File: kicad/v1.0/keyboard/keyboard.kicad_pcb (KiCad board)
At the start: 2 copper layers, 124 parts, among them J1 NumPad, J2 PMOD, SW1 KeyButton, SW10 KeyButton, SW11 KeyButton, SW12 KeyButton, SW13 KeyButton, SW14 KeyButton, SW15 KeyButton, SW16 KeyButton, SW17 KeyButton, SW18 KeyButton, SW19 KeyButton, SW2 KeyButton, SW20 KeyButton, SW21 KeyButton, SW22 KeyButton, SW23 KeyButton, SW24 KeyButton, SW25 KeyButton, SW26 KeyButton, SW27 KeyButton, SW3 KeyButton, SW33 KeyButton, SW34 KeyButton, SW35 KeyButton, SW36 KeyButton, SW37 KeyButton, SW38 KeyButton, SW39 KeyButton, SW4 KeyButton, SW40 KeyButton, SW41 KeyButton, SW42 KeyButton, SW43 KeyButton, SW44 KeyButton, SW45 KeyButton, SW46 KeyButton, SW47 KeyButton, SW48 KeyButton, SW49 KeyButton, SW5 KeyButton, SW50 KeyButton, SW51 KeyButton, SW52 KeyButton, SW53 KeyButton, SW54 KeyButton, SW55 KeyButton, SW56 KeyButton, SW57 KeyButton, SW58 KeyButton, SW59 KeyButton, SW6 KeyButton, SW7 KeyButton, SW8 KeyButton, SW9 KeyButton, U1 74LS165, U2 74LS165, U3 74LS165, U4 74LS165, U5 74LS165, U6 74LS165, U7 74LS165

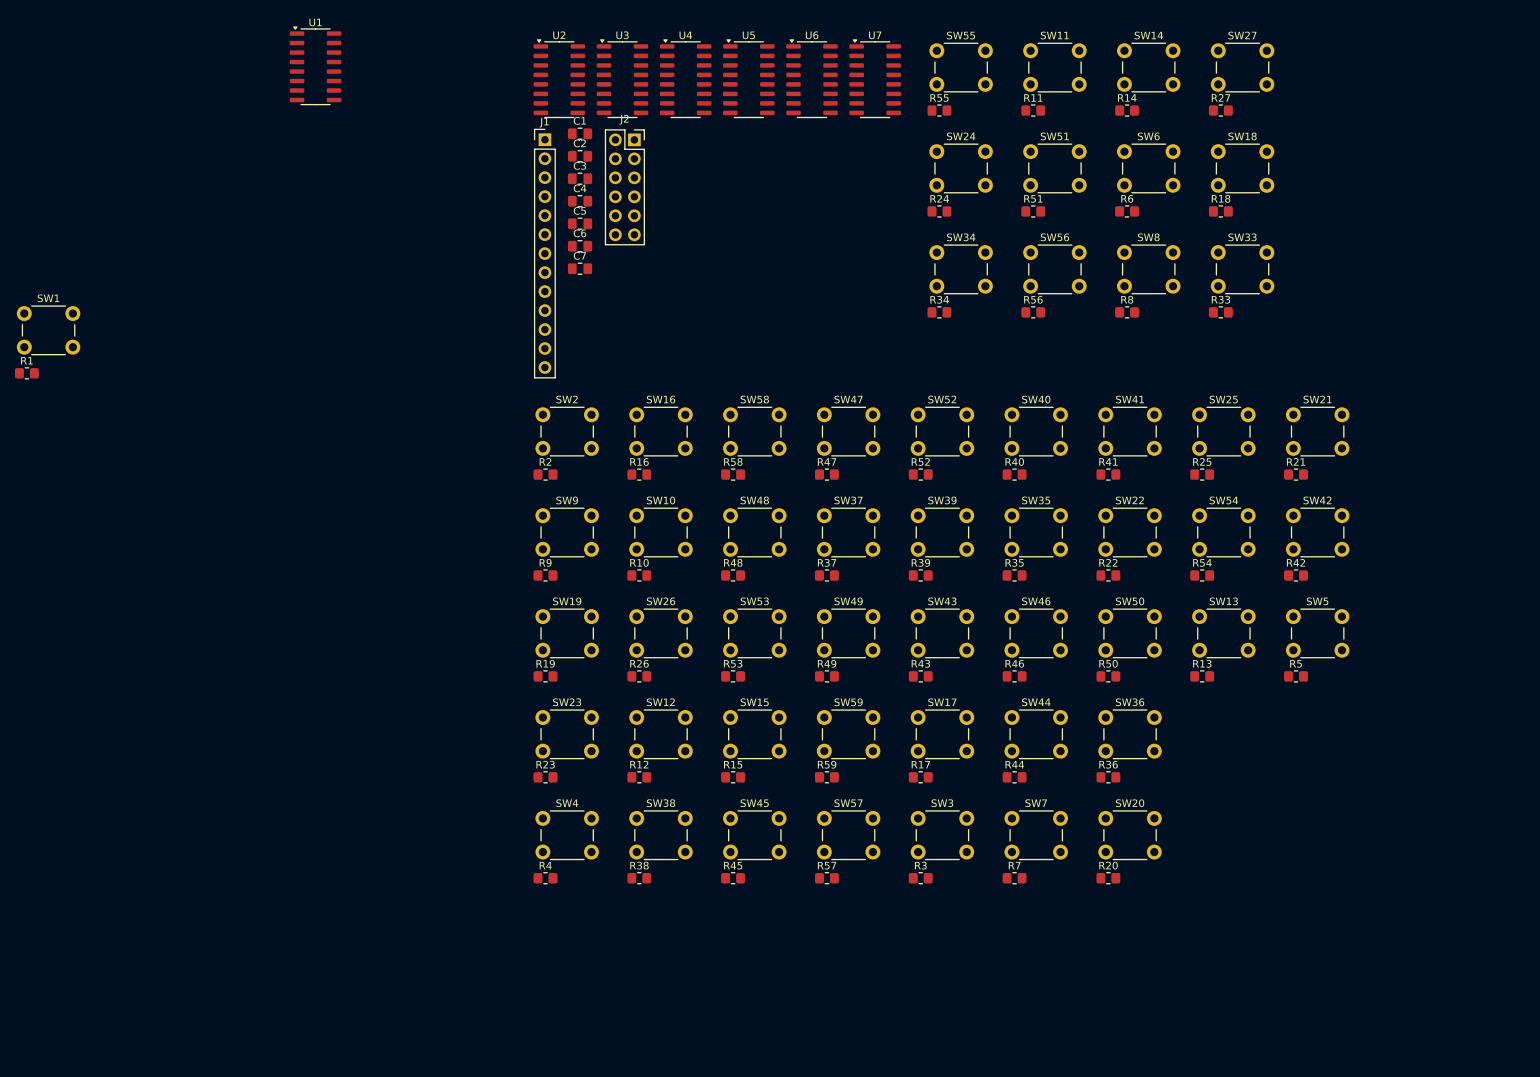
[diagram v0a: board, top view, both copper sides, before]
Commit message: Positioning
- Added Library
- Created Footprint for 2-pin push-button
- Added additional keys for ENTER and SPACE to cover whole length
- Added keys for numpad (1:1 link to other number keys)
- Positioned main keys, numpad keys
- Created cutout for reset switch
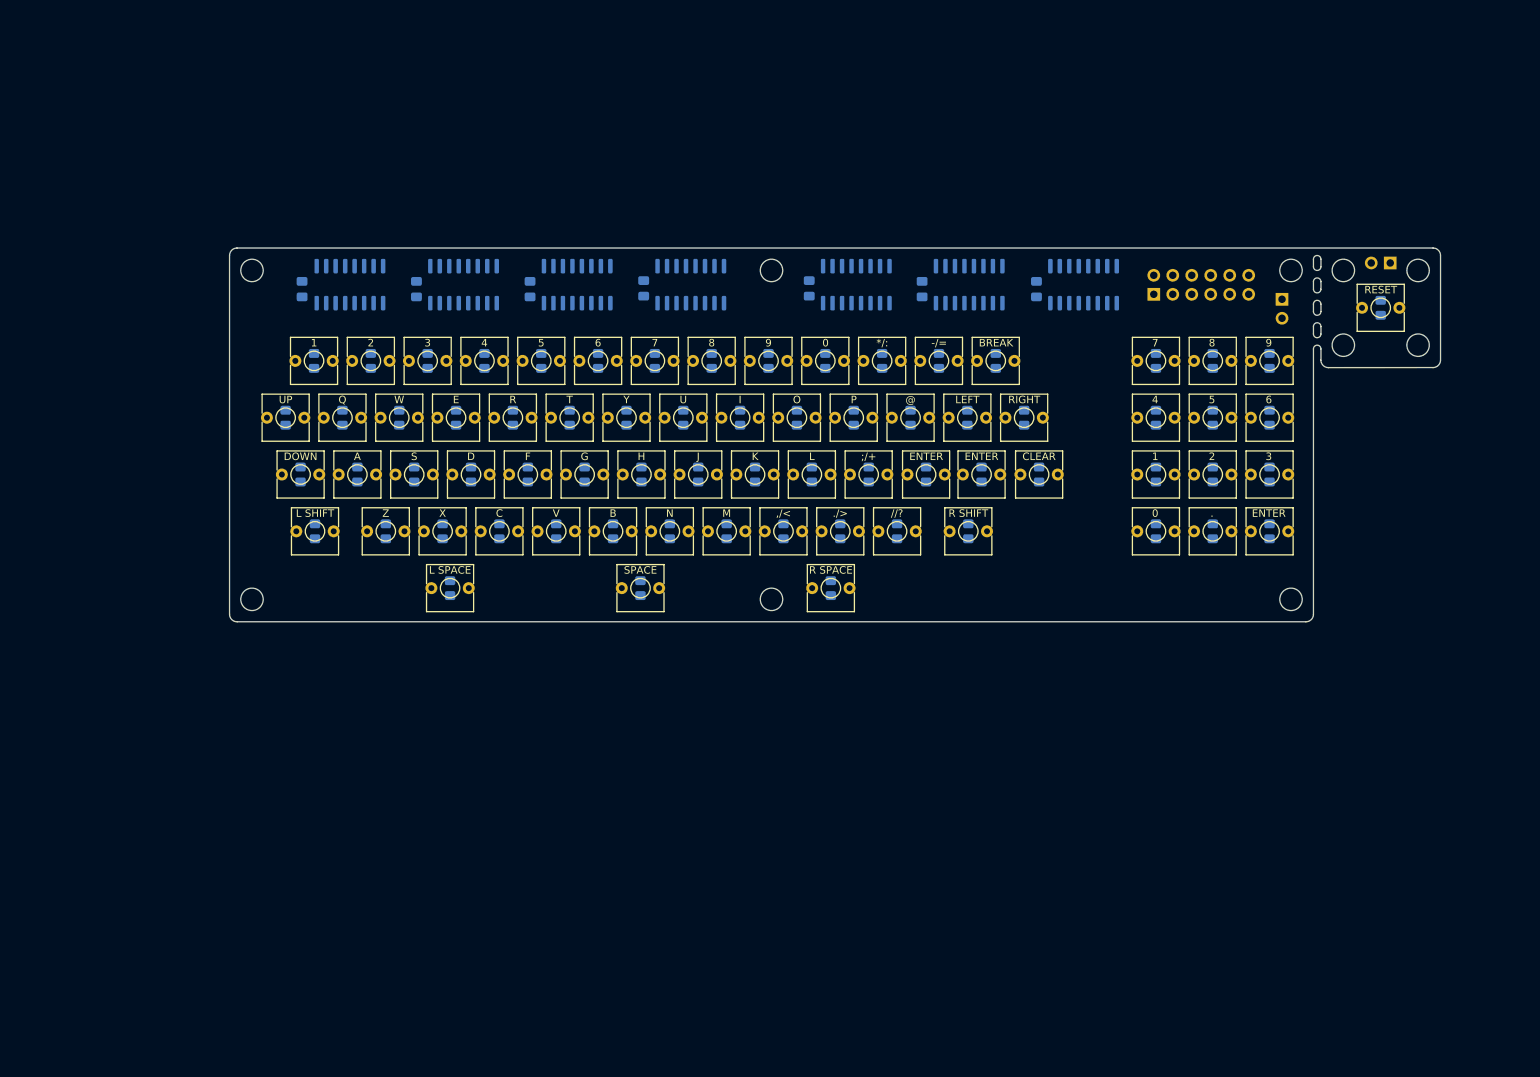
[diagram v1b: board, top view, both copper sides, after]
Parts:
- added J3: Conn_01x02, Connector_PinHeader_2.54mm:PinHeader_1x02_P2.54mm_Vertical, B.Cu at (224.5, 75.5)
- added R60: 4K7, Resistor_SMD:R_0805_2012Metric_Pad1.20x1.40mm_HandSolder, B.Cu at (169.9, 103.8)
- added R61: 4K7, Resistor_SMD:R_0805_2012Metric_Pad1.20x1.40mm_HandSolder, B.Cu at (124.2, 119.0)
- added R62: 4K7, Resistor_SMD:R_0805_2012Metric_Pad1.20x1.40mm_HandSolder, B.Cu at (149.7, 119.0)
- added R63: 4K7, Resistor_SMD:R_0805_2012Metric_Pad1.20x1.40mm_HandSolder, B.Cu at (193.2, 103.8)
- added R64: 4K7, Resistor_SMD:R_0805_2012Metric_Pad1.20x1.40mm_HandSolder, B.Cu at (193.2, 111.4)
- added R65: 4K7, Resistor_SMD:R_0805_2012Metric_Pad1.20x1.40mm_HandSolder, B.Cu at (200.8, 103.8)
- added R66: 4K7, Resistor_SMD:R_0805_2012Metric_Pad1.20x1.40mm_HandSolder, B.Cu at (208.4, 103.8)
- added R67: 4K7, Resistor_SMD:R_0805_2012Metric_Pad1.20x1.40mm_HandSolder, B.Cu at (193.2, 96.2)
- added R68: 4K7, Resistor_SMD:R_0805_2012Metric_Pad1.20x1.40mm_HandSolder, B.Cu at (200.8, 96.2)
- added R69: 4K7, Resistor_SMD:R_0805_2012Metric_Pad1.20x1.40mm_HandSolder, B.Cu at (208.4, 96.2)
- added R70: 4K7, Resistor_SMD:R_0805_2012Metric_Pad1.20x1.40mm_HandSolder, B.Cu at (193.2, 88.6)
- added R71: 4K7, Resistor_SMD:R_0805_2012Metric_Pad1.20x1.40mm_HandSolder, B.Cu at (208.4, 88.6)
- added R72: 4K7, Resistor_SMD:R_0805_2012Metric_Pad1.20x1.40mm_HandSolder, B.Cu at (200.8, 88.6)
- added R73: 4K7, Resistor_SMD:R_0805_2012Metric_Pad1.20x1.40mm_HandSolder, B.Cu at (200.8, 111.4)
- added R74: 4K7, Resistor_SMD:R_0805_2012Metric_Pad1.20x1.40mm_HandSolder, B.Cu at (208.4, 111.4)
- added SW60: KeyButton, Library:SW_SPST_Push, F.Cu at (169.9, 103.8)
- added SW61: KeyButton, Library:SW_SPST_Push, F.Cu at (124.2, 119.0)
- added SW62: KeyButton, Library:SW_SPST_Push, F.Cu at (149.7, 119.0)
- added SW63: KeyButton, Library:SW_SPST_Push, F.Cu at (193.2, 103.8)
- added SW64: KeyButton, Library:SW_SPST_Push, F.Cu at (193.2, 111.4)
- added SW65: KeyButton, Library:SW_SPST_Push, F.Cu at (200.8, 103.8)
- added SW66: KeyButton, Library:SW_SPST_Push, F.Cu at (208.4, 103.8)
- added SW67: KeyButton, Library:SW_SPST_Push, F.Cu at (193.2, 96.2)
- added SW68: KeyButton, Library:SW_SPST_Push, F.Cu at (200.8, 96.2)
- added SW69: KeyButton, Library:SW_SPST_Push, F.Cu at (208.4, 96.2)
- added SW70: KeyButton, Library:SW_SPST_Push, F.Cu at (193.2, 88.6)
- added SW71: KeyButton, Library:SW_SPST_Push, F.Cu at (208.4, 88.6)
- added SW72: KeyButton, Library:SW_SPST_Push, F.Cu at (200.8, 88.6)
- added SW73: KeyButton, Library:SW_SPST_Push, F.Cu at (200.8, 111.4)
- added SW74: KeyButton, Library:SW_SPST_Push, F.Cu at (208.4, 111.4)
- C1, C2, C3, C4, C5, C6, C7, R1, R10, R11, R12, R13, R14, R15, R16, R17, R18, R19, R2, R20, R21, R22, R23, R24, R25, R26, R27, R3, R33, R34, R35, R36, R37, R38, R39, R4, R40, R41, R42, R43, R44, R45, R46, R47, R48, R49, R5, R50, R51, R52, R53, R54, R55, R56, R57, R58, R59, R6, R7, R8, R9, U1, U2, U3, U4, U5, U6, U7: moved to B.Cu
- J1: value NumPad -> PMOD; footprint Connector_PinHeader_2.54mm:PinHeader_1x13_P2.54mm_Vertical -> Connector_PinSocket_2.54mm:PinSocket_2x06_P2.54mm_Vertical; moved to B.Cu
- J2: value PMOD -> Conn_01x02; footprint Connector_PinSocket_2.54mm:PinSocket_2x06_P2.54mm_Vertical -> Connector_PinHeader_2.54mm:PinHeader_1x02_P2.54mm_Vertical; moved to B.Cu
- SW1, SW10, SW11, SW12, SW13, SW14, SW15, SW16, SW17, SW18, SW19, SW2, SW20, SW21, SW22, SW23, SW24, SW25, SW26, SW27, SW3, SW33, SW34, SW35, SW36, SW37, SW38, SW39, SW4, SW40, SW41, SW42, SW43, SW44, SW45, SW46, SW47, SW48, SW49, SW5, SW50, SW51, SW52, SW53, SW54, SW55, SW56, SW57, SW58, SW59, SW6, SW7, SW8, SW9: footprint Button_Switch_THT:SW_PUSH_6mm -> Library:SW_SPST_Push
- moved SW27 128.6 mm to (90.2, 111.4)
- moved R27 125.1 mm to (90.2, 111.4), turned to 90 degrees
- moved SW33 121.8 mm to (80.6, 88.6)
- moved R33 121.5 mm to (80.6, 88.6), turned to 90 degrees
- moved SW1 119.4 mm to (160.4, 96.2)
- moved R1 118.4 mm to (160.4, 96.2), turned to 90 degrees
- moved R5 113.6 mm to (101.6, 103.8), turned to 90 degrees
- moved SW5 111.6 mm to (101.6, 103.8)
- moved R20 107.4 mm to (94.0, 103.8), turned to 90 degrees
- moved R36 106.8 mm to (95.8, 88.6), turned to 90 degrees
- moved SW20 103.3 mm to (94.0, 103.8)
- moved SW36 102.5 mm to (95.8, 88.6)
- moved R21 97.5 mm to (114.8, 96.2), turned to 90 degrees
- moved R59 97.1 mm to (223.3, 81.5), turned to 90 degrees
- moved SW21 96.8 mm to (114.8, 96.2)
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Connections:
- J1 pad 1: unconnected-(J1-Pin_1-Pad1) -> PMOD_IO1
- J1 pad 10: unconnected-(J1-Pin_10-Pad10) -> GND
- J1 pad 11: unconnected-(J1-Pin_11-Pad11) -> +3V3
- J1 pad 12: unconnected-(J1-Pin_12-Pad12) -> +3V3
- J1 pad 2: unconnected-(J1-Pin_2-Pad2) -> PMOD_IO5
- J1 pad 3: unconnected-(J1-Pin_3-Pad3) -> PMOD_IO2
- J1 pad 4: unconnected-(J1-Pin_4-Pad4) -> PMOD_IO6
- J1 pad 5: unconnected-(J1-Pin_5-Pad5) -> PMOD_IO3
- J1 pad 6: unconnected-(J1-Pin_6-Pad6) -> PMOD_IO7
- J1 pad 7: unconnected-(J1-Pin_7-Pad7) -> PMOD_IO4
- J1 pad 8: unconnected-(J1-Pin_8-Pad8) -> PMOD_IO8
- J1 pad 9: unconnected-(J1-Pin_9-Pad9) -> GND
- J2 pad 1: PMOD_IO1 -> unconnected-(J2-Pin_1-Pad1)
- J2 pad 2: PMOD_IO5 -> GND
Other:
- board outline added: 162 x 50 mm
- board text added: "*/:"
- board text added: ",/<"
- board text added: "-/="
- board text added: "."
- board text added: "./>"
- board text added: "//?"
- board text added: "0"
- board text added: "1"
- board text added: "2"
- board text added: "3"
- board text added: "4"
- board text added: "5"
- board text added: "6"
- board text added: "7"
- board text added: "8"
- board text added: "9"
- board text added: ";/+"
- board text added: "@"
- board text added: "A"
- board text added: "B"
- board text added: "BREAK"
- board text added: "C"
- board text added: "CLEAR"
- board text added: "D"
- board text added: "DOWN"
- board text added: "E"
- board text added: "ENTER"
- board text added: "F"
- board text added: "G"
- board text added: "H"
- board text added: "I"
- board text added: "J"
- board text added: "K"
- board text added: "L"
- board text added: "L SHIFT"
- board text added: "L SPACE"
- board text added: "LEFT"
- board text added: "M"
- board text added: "N"
- board text added: "O"
- board text added: "P"
- board text added: "Q"
- board text added: "R"
- board text added: "R SHIFT"
- board text added: "R SPACE"
- board text added: "RESET"
- board text added: "RIGHT"
- board text added: "S"
- board text added: "SPACE"
- board text added: "T"
- board text added: "U"
- board text added: "UP"
- board text added: "V"
- board text added: "W"
- board text added: "X"
- board text added: "Y"
- board text added: "Z"

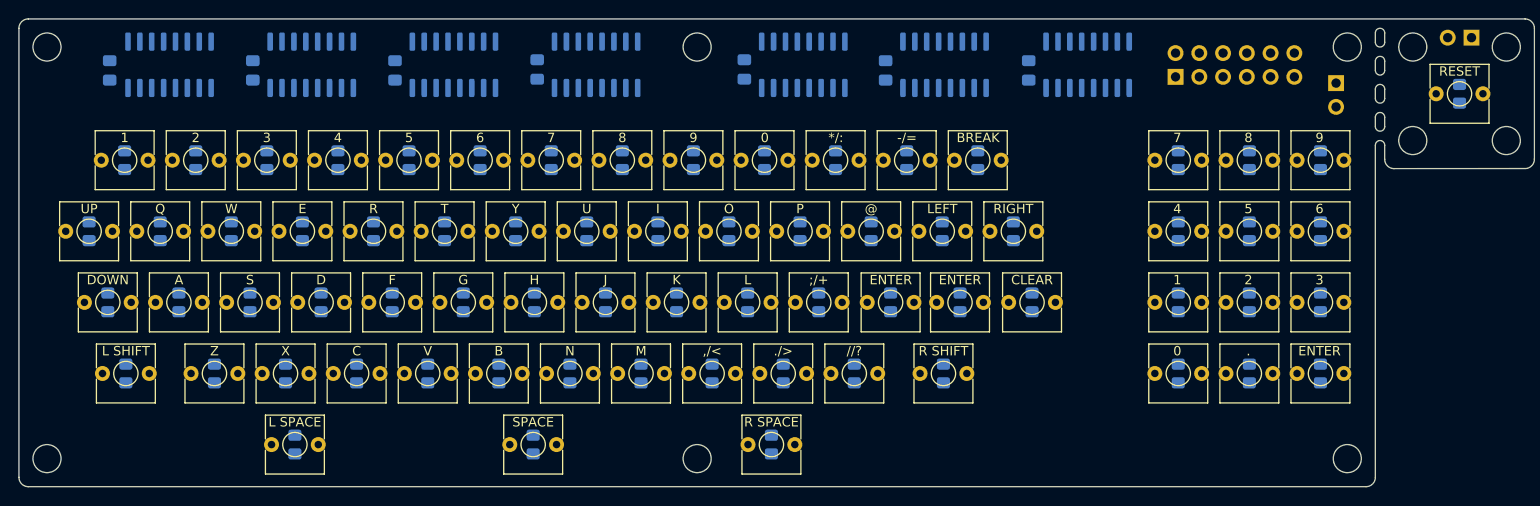
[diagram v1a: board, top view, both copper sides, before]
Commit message: Redesign of Keyboard
This is a new design of the keyboard that is based on the TRS-80 Model 1 keyboard interface design.
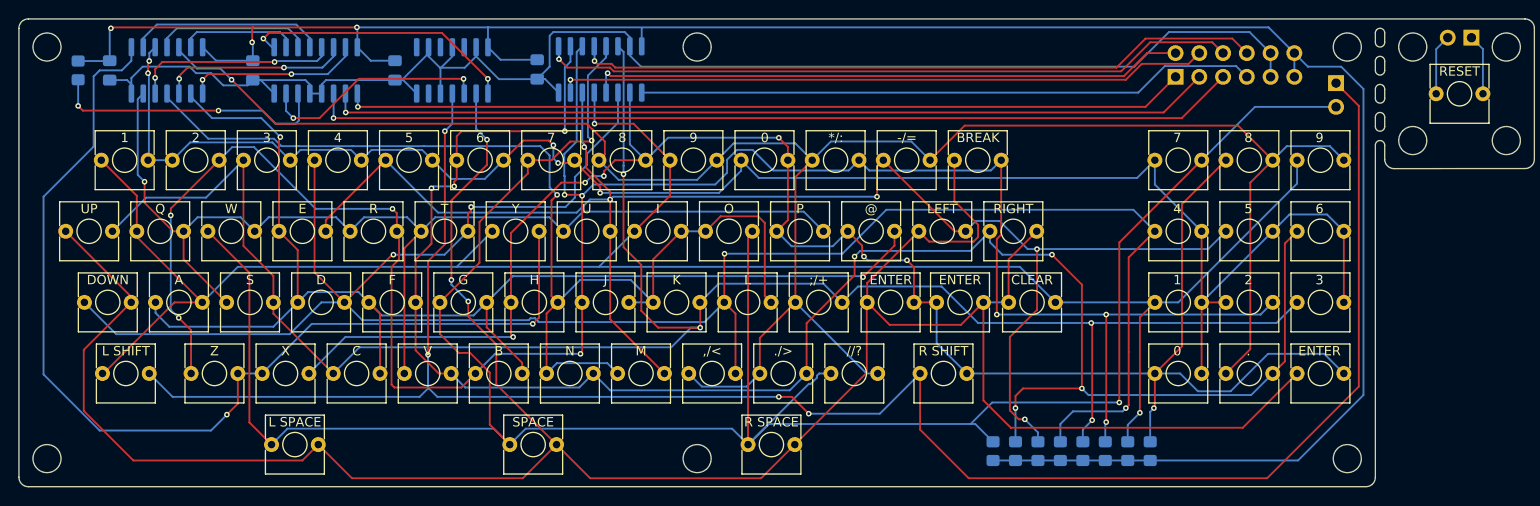
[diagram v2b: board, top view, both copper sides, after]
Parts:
- removed C5, C6, C7: 0.1uF, Capacitor_SMD:C_0805_2012Metric_Pad1.18x1.45mm_HandSolder
- removed R10, R11, R12, R13, R14, R15, R16, R17, R18, R19, R20, R21, R22, R23, R24, R25, R26, R27, R33, R34, R35, R36, R37, R38, R39, R40, R41, R42, R43, R44, R45, R46, R47, R48, R49, R50, R51, R52, R53, R54, R55, R56, R57, R58, R59, R60, R61, R62, R63, R64, R65, R66, R67, R68, R69, R70, R71, R72, R73, R74: 4K7, Resistor_SMD:R_0805_2012Metric_Pad1.20x1.40mm_HandSolder
- removed U5, U6, U7: 74LS165, Package_SO:SOIC-16_3.9x9.9mm_P1.27mm
- R1, R2, R3, R4, R5, R6, R7, R8, R9: value 4K7 -> 1k
- SW1: value KeyButton -> @
- SW10: renamed from SW9; value KeyButton -> I
- SW11: value KeyButton -> J
- SW12: value KeyButton -> K
- SW13: value KeyButton -> L
- SW14: value KeyButton -> M
- SW15: value KeyButton -> N
- SW16: value KeyButton -> O
- SW17: renamed from SW18; value KeyButton -> P
- SW18: renamed from SW17; value KeyButton -> Q
- SW19: value KeyButton -> R
- SW2: value KeyButton -> A
- SW20: value KeyButton -> S
- SW21: value KeyButton -> T
- SW22: value KeyButton -> U
- SW23: value KeyButton -> V
- SW24: value KeyButton -> W
- SW25: renamed from SW26; value KeyButton -> X
- SW26: renamed from SW25; value KeyButton -> Y
- SW27: value KeyButton -> Z
- SW28: renamed from SW64; value KeyButton -> 0
- SW29: renamed from SW63; value KeyButton -> 1
- SW3: value KeyButton -> B
- SW30: renamed from SW65; value KeyButton -> 2
- SW31: renamed from SW66; value KeyButton -> 3
- SW32: renamed from SW67; value KeyButton -> 4
- SW33: renamed from SW68; value KeyButton -> 5
- SW34: renamed from SW69; value KeyButton -> 6
- SW35: renamed from SW70; value KeyButton -> 7
- SW36: renamed from SW34; value KeyButton -> 0
- SW37: renamed from SW33; value KeyButton -> 1
- SW38: renamed from SW35; value KeyButton -> 2
- SW39: renamed from SW36; value KeyButton -> 3
- SW4: value KeyButton -> C
- SW40: renamed from SW37; value KeyButton -> 4
- SW41: renamed from SW38; value KeyButton -> 5
- SW42: renamed from SW39; value KeyButton -> 6
- SW43: renamed from SW40; value KeyButton -> 7
- SW44: renamed from SW72; value KeyButton -> 8
- SW45: renamed from SW71; value KeyButton -> 9
- SW46: renamed from SW73; value KeyButton -> .
- SW47: renamed from SW42; value KeyButton -> 8
- SW48: renamed from SW41; value KeyButton -> 9
- SW49: renamed from SW43; value KeyButton -> :
- SW5: value KeyButton -> D
- SW50: renamed from SW44; value KeyButton -> ;
- SW51: renamed from SW45; value KeyButton -> ,
- SW52: renamed from SW46; value KeyButton -> -
- SW53: renamed from SW47; value KeyButton -> .
- SW54: renamed from SW48; value KeyButton -> /
- SW55: renamed from SW50; value KeyButton -> ENTER
- SW56: renamed from SW60; value KeyButton -> ENTER
- SW57: renamed from SW49; value KeyButton -> CLEAR
- SW58: renamed from SW51; value KeyButton -> BREAK
- SW59: renamed from SW52; value KeyButton -> UP
- SW6: value KeyButton -> E
- SW60: renamed from SW53; value KeyButton -> DOWN
- SW61: renamed from SW54; value KeyButton -> LEFT
- SW62: renamed from SW55; value KeyButton -> RIGHT
- SW63: renamed from SW61; value KeyButton -> SPACE
- SW64: renamed from SW59; value KeyButton -> RESET
- SW65: renamed from SW57; value KeyButton -> RSHIFT
- SW66: renamed from SW58; value KeyButton -> LSHIFT
- SW67: renamed from SW56; value KeyButton -> SPACE
- SW68: renamed from SW62; value KeyButton -> SPACE
- SW69: renamed from SW74; value KeyButton -> ENTER
- SW7: value KeyButton -> F
- SW8: value KeyButton -> G
- SW9: renamed from SW10; value KeyButton -> H
- U1, U3: value 74LS165 -> 74LS07; footprint Package_SO:SOIC-16_3.9x9.9mm_P1.27mm -> Package_SO:SOIC-14_3.9x8.7mm_P1.27mm
- U2: value 74LS165 -> 74LS138
- U4: value 74LS165 -> 74LS157
- moved R2 105.0 mm to (190.2, 119.7)
- moved R1 86.5 mm to (75.6, 79.0), turned to -90 degrees
- moved R6 84.4 mm to (180.6, 119.7)
- moved R5 83.0 mm to (183.0, 119.7)
- moved R4 80.5 mm to (185.4, 119.7)
- moved R7 70.8 mm to (178.2, 119.7)
- moved R3 67.7 mm to (187.8, 119.7)
- moved R8 61.1 mm to (175.8, 119.7)
- moved R9 42.8 mm to (173.4, 119.7)
- moved U2 0.74 mm to (101.0, 79.0), turned to 90 degrees
- moved U4 0.66 mm to (131.4, 78.9), turned to 90 degrees
- moved U1 0.66 mm to (85.1, 79.0), turned to 90 degrees
- moved U3 0.62 mm to (115.6, 79.0), turned to 90 degrees
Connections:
- net KEY_RESET renamed Net-(J3-Pin_1)
- C1 pad 1: GND -> +3.3V
- C1 pad 2: +3V3 -> GND
- C2 pad 1: GND -> +3.3V
- C2 pad 2: +3V3 -> GND
- C3 pad 1: GND -> +3.3V
- C3 pad 2: +3V3 -> GND
- C4 pad 1: GND -> +3.3V
- C4 pad 2: +3V3 -> GND
- J1 pad 11: +3V3 -> +3.3V
- J1 pad 12: +3V3 -> +3.3V
- J2 pad 1: unconnected-(J2-Pin_1-Pad1) -> Net-(J2-Pin_1)
- J2 pad 2: GND -> Net-(J2-Pin_2)
- J3 pad 2: GND -> Net-(J3-Pin_2)
- R1 pad 1: +3V3 -> +3.3V
- R1 pad 2: KEY_AT -> Net-(U2-E3)
- R2 pad 1: +3V3 -> +3.3V
- R2 pad 2: KEY_A -> Net-(U4-I0a)
- R3 pad 1: +3V3 -> +3.3V
- R3 pad 2: KEY_B -> Net-(U4-I0b)
- R4 pad 1: +3V3 -> +3.3V
- R4 pad 2: KEY_C -> Net-(U4-I0c)
- R5 pad 1: +3V3 -> +3.3V
- R5 pad 2: KEY_D -> Net-(U4-I0d)
- R6 pad 1: +3V3 -> +3.3V
- R6 pad 2: KEY_E -> Net-(U4-I1a)
- R7 pad 1: +3V3 -> +3.3V
- R7 pad 2: KEY_F -> Net-(U4-I1b)
- R8 pad 1: +3V3 -> +3.3V
- R8 pad 2: KEY_G -> Net-(U4-I1c)
- R9 pad 1: +3V3 -> +3.3V
- R9 pad 2: KEY_I -> Net-(J2-Pin_2)
- SW1 pad 1: GND -> Net-(U4-I0a)
- SW1 pad 2: KEY_AT -> Net-(SW1-Pad2)
- SW10 pad 1: GND -> Net-(U4-I0b)
- SW10 pad 2: KEY_I -> Net-(SW10-Pad2)
- SW11 pad 1: GND -> Net-(U4-I0c)
- SW11 pad 2: KEY_J -> Net-(SW10-Pad2)
- SW12 pad 1: GND -> Net-(SW10-Pad2)
- SW12 pad 2: KEY_K -> Net-(U4-I0d)
- SW13 pad 1: GND -> Net-(U4-I1a)
- SW13 pad 2: KEY_L -> Net-(SW10-Pad2)
- SW14 pad 1: GND -> Net-(SW10-Pad2)
- SW14 pad 2: KEY_M -> Net-(U4-I1b)
- SW15 pad 1: GND -> Net-(SW10-Pad2)
- SW15 pad 2: KEY_N -> Net-(U4-I1c)
- SW16 pad 1: GND -> Net-(SW10-Pad2)
- SW16 pad 2: KEY_O -> Net-(J2-Pin_2)
- SW17 pad 1: GND -> Net-(U4-I0a)
- SW17 pad 2: KEY_P -> Net-(SW17-Pad2)
- SW18 pad 1: GND -> Net-(U4-I0b)
- SW18 pad 2: KEY_Q -> Net-(SW17-Pad2)
- SW19 pad 1: GND -> Net-(SW17-Pad2)
- SW19 pad 2: KEY_R -> Net-(U4-I0c)
- SW2 pad 1: GND -> Net-(SW1-Pad2)
- SW2 pad 2: KEY_A -> Net-(U4-I0b)
- SW20 pad 1: GND -> Net-(SW17-Pad2)
- SW20 pad 2: KEY_S -> Net-(U4-I0d)
- SW21 pad 1: GND -> Net-(SW17-Pad2)
- SW21 pad 2: KEY_T -> Net-(U4-I1a)
- SW22 pad 1: GND -> Net-(SW17-Pad2)
- SW22 pad 2: KEY_U -> Net-(U4-I1b)
- SW23 pad 1: GND -> Net-(SW17-Pad2)
- SW23 pad 2: KEY_V -> Net-(U4-I1c)
- SW24 pad 1: GND -> Net-(J2-Pin_2)
- SW24 pad 2: KEY_W -> Net-(SW17-Pad2)
- SW25 pad 1: GND -> Net-(SW25-Pad1)
- SW25 pad 2: KEY_X -> Net-(U4-I0a)
- SW26 pad 1: GND -> Net-(U4-I0b)
- SW26 pad 2: KEY_Y -> Net-(SW25-Pad1)
- SW27 pad 1: GND -> Net-(U4-I0c)
- SW27 pad 2: KEY_Z -> Net-(SW25-Pad1)
- SW28 pad 1: GND -> Net-(U4-I0a)
- SW28 pad 2: KEY_0 -> Net-(SW28-Pad2)
- SW29 pad 1: GND -> Net-(U4-I0b)
- SW29 pad 2: KEY_1 -> Net-(SW28-Pad2)
- SW3 pad 1: GND -> Net-(U4-I0c)
- SW3 pad 2: KEY_B -> Net-(SW1-Pad2)
- SW30 pad 1: GND -> Net-(SW28-Pad2)
- SW30 pad 2: KEY_2 -> Net-(U4-I0c)
- SW31 pad 1: GND -> Net-(U4-I0d)
- SW31 pad 2: KEY_3 -> Net-(SW28-Pad2)
- SW32 pad 1: GND -> Net-(U4-I1a)
- SW32 pad 2: KEY_4 -> Net-(SW28-Pad2)
- SW33 pad 1: GND -> Net-(U4-I1b)
- SW33 pad 2: KEY_5 -> Net-(SW28-Pad2)
- SW34 pad 1: GND -> Net-(U4-I1c)
- SW34 pad 2: KEY_6 -> Net-(SW28-Pad2)
- SW35 pad 1: GND -> Net-(SW28-Pad2)
- SW35 pad 2: KEY_7 -> Net-(J2-Pin_2)
- SW36 pad 1: GND -> Net-(SW28-Pad2)
- SW36 pad 2: KEY_0 -> Net-(U4-I0a)
- SW37 pad 1: GND -> Net-(U4-I0b)
- SW37 pad 2: KEY_1 -> Net-(SW28-Pad2)
- SW38 pad 1: GND -> Net-(SW28-Pad2)
- SW38 pad 2: KEY_2 -> Net-(U4-I0c)
- SW39 pad 1: GND -> Net-(U4-I0d)
- SW39 pad 2: KEY_3 -> Net-(SW28-Pad2)
- SW4 pad 1: GND -> Net-(U4-I0d)
- SW4 pad 2: KEY_C -> Net-(SW1-Pad2)
- SW40 pad 1: GND -> Net-(U4-I1a)
- SW40 pad 2: KEY_4 -> Net-(SW28-Pad2)
- SW41 pad 1: GND -> Net-(U4-I1b)
- SW41 pad 2: KEY_5 -> Net-(SW28-Pad2)
- SW42 pad 1: GND -> Net-(U4-I1c)
- SW42 pad 2: KEY_6 -> Net-(SW28-Pad2)
- SW43 pad 1: GND -> Net-(J2-Pin_2)
- SW43 pad 2: KEY_7 -> Net-(SW28-Pad2)
- SW44 pad 1: GND -> Net-(U4-I0a)
- SW44 pad 2: KEY_8 -> Net-(SW44-Pad2)
- SW45 pad 1: GND -> Net-(U4-I0b)
- SW45 pad 2: KEY_9 -> Net-(SW44-Pad2)
- SW46 pad 1: GND -> Net-(SW44-Pad2)
- SW46 pad 2: KEY_DOT -> Net-(U4-I1c)
- SW47 pad 1: GND -> Net-(SW44-Pad2)
- SW47 pad 2: KEY_8 -> Net-(U4-I0a)
- SW48 pad 1: GND -> Net-(U4-I0b)
- SW48 pad 2: KEY_9 -> Net-(SW44-Pad2)
- SW49 pad 1: GND -> Net-(SW44-Pad2)
- SW49 pad 2: KEY_COLON -> Net-(U4-I0c)
- SW5 pad 1: GND -> Net-(SW1-Pad2)
- SW5 pad 2: KEY_D -> Net-(U4-I1a)
- SW50 pad 1: GND -> Net-(SW44-Pad2)
- SW50 pad 2: KEY_SEMICOLON -> Net-(U4-I0d)
- SW51 pad 1: GND -> Net-(SW44-Pad2)
- SW51 pad 2: KEY_COMMA -> Net-(U4-I1a)
- SW52 pad 1: GND -> Net-(U4-I1b)
- SW52 pad 2: KEY_MINUS -> Net-(SW44-Pad2)
- SW53 pad 1: GND -> Net-(SW44-Pad2)
- SW53 pad 2: KEY_DOT -> Net-(U4-I1c)
- SW54 pad 1: GND -> Net-(J2-Pin_2)
- SW54 pad 2: KEY_SLASH -> Net-(SW44-Pad2)
- SW55 pad 1: GND -> Net-(SW55-Pad1)
- SW55 pad 2: KEY_ENTER -> Net-(U4-I0a)
- SW56 pad 1: GND -> Net-(U4-I0a)
- SW56 pad 2: KEY_ENTER -> Net-(SW55-Pad1)
- SW57 pad 1: GND -> Net-(SW55-Pad1)
- SW57 pad 2: KEY_CLEAR -> Net-(U4-I0b)
- SW58 pad 1: GND -> Net-(SW55-Pad1)
- SW58 pad 2: KEY_BREAK -> Net-(U4-I0c)
- SW59 pad 1: GND -> Net-(SW55-Pad1)
- SW59 pad 2: KEY_UP -> Net-(U4-I0d)
- SW6 pad 1: GND -> Net-(SW1-Pad2)
- SW6 pad 2: KEY_E -> Net-(U4-I1b)
- SW60 pad 1: GND -> Net-(U4-I1a)
- SW60 pad 2: KEY_DOWN -> Net-(SW55-Pad1)
- SW61 pad 1: GND -> Net-(SW55-Pad1)
- SW61 pad 2: KEY_LEFT -> Net-(U4-I1b)
- SW62 pad 1: GND -> Net-(U4-I1c)
- SW62 pad 2: KEY_RIGHT -> Net-(SW55-Pad1)
- SW63 pad 1: GND -> Net-(J2-Pin_2)
- SW63 pad 2: KEY_SPACE -> Net-(SW55-Pad1)
- SW64 pad 1: GND -> Net-(J3-Pin_2)
- SW65 pad 1: GND -> Net-(J2-Pin_1)
- SW65 pad 2: KEY_RSHIFT -> Net-(U4-I0a)
- SW66 pad 1: GND -> Net-(U4-I0b)
- SW66 pad 2: KEY_LSHIFT -> Net-(J2-Pin_1)
- SW67 pad 1: GND -> Net-(J2-Pin_2)
- SW67 pad 2: KEY_SPACE -> Net-(SW55-Pad1)
- SW68 pad 1: GND -> Net-(J2-Pin_2)
- SW68 pad 2: KEY_SPACE -> Net-(SW55-Pad1)
- SW69 pad 1: GND -> Net-(SW55-Pad1)
- SW69 pad 2: KEY_ENTER -> Net-(U4-I0a)
- SW7 pad 1: GND -> Net-(SW1-Pad2)
- SW7 pad 2: KEY_F -> Net-(U4-I1c)
- SW8 pad 1: GND -> Net-(J2-Pin_2)
- SW8 pad 2: KEY_G -> Net-(SW1-Pad2)
- SW9 pad 1: GND -> Net-(U4-I0a)
- SW9 pad 2: KEY_H -> Net-(SW10-Pad2)
- U1 pad 1: unconnected-(U1-~{PL}-Pad1) -> Net-(U2-O0)
- U1 pad 10: unconnected-(U1-DS-Pad10) -> Net-(SW28-Pad2)
- U1 pad 11: unconnected-(U1-D0-Pad11) -> Net-(U2-O4)
- U1 pad 12: unconnected-(U1-D1-Pad12) -> Net-(SW44-Pad2)
- U1 pad 13: unconnected-(U1-D2-Pad13) -> Net-(U2-O5)
- U1 pad 14: unconnected-(U1-D3-Pad14) -> +3.3V
- U1 pad 2: unconnected-(U1-CP-Pad2) -> Net-(SW1-Pad2)
- U1 pad 3: unconnected-(U1-D4-Pad3) -> Net-(U2-O1)
- U1 pad 4: unconnected-(U1-D5-Pad4) -> Net-(SW10-Pad2)
- U1 pad 5: unconnected-(U1-D6-Pad5) -> Net-(U2-O2)
- U1 pad 6: unconnected-(U1-D7-Pad6) -> Net-(SW17-Pad2)
- U1 pad 7: unconnected-(U1-~{Q7}-Pad7) -> GND
- U1 pad 8: GND -> Net-(SW25-Pad1)
- U1 pad 9: unconnected-(U1-Q7-Pad9) -> Net-(U2-O3)
- U2 pad 1: unconnected-(U2-~{PL}-Pad1) -> PMOD_IO1
- U2 pad 10: unconnected-(U2-DS-Pad10) -> Net-(U2-O5)
- U2 pad 11: unconnected-(U2-D0-Pad11) -> Net-(U2-O4)
- U2 pad 12: unconnected-(U2-D1-Pad12) -> Net-(U2-O3)
- U2 pad 13: unconnected-(U2-D2-Pad13) -> Net-(U2-O2)
- U2 pad 14: unconnected-(U2-D3-Pad14) -> Net-(U2-O1)
- U2 pad 15: unconnected-(U2-~{CE}-Pad15) -> Net-(U2-O0)
- U2 pad 16: +3V3 -> +3.3V
- U2 pad 2: unconnected-(U2-CP-Pad2) -> PMOD_IO2
- U2 pad 3: unconnected-(U2-D4-Pad3) -> PMOD_IO3
- U2 pad 4: unconnected-(U2-D5-Pad4) -> GND
- U2 pad 5: unconnected-(U2-D6-Pad5) -> GND
- U2 pad 6: unconnected-(U2-D7-Pad6) -> Net-(U2-E3)
- U2 pad 7: unconnected-(U2-~{Q7}-Pad7) -> Net-(U2-O7)
- U2 pad 9: unconnected-(U2-Q7-Pad9) -> Net-(U2-O6)
- U3 pad 1: unconnected-(U3-~{PL}-Pad1) -> Net-(U2-O6)
- U3 pad 11: unconnected-(U3-D0-Pad11) -> GND
- U3 pad 13: unconnected-(U3-D2-Pad13) -> GND
- U3 pad 14: unconnected-(U3-D3-Pad14) -> +3.3V
- U3 pad 2: unconnected-(U3-CP-Pad2) -> Net-(SW55-Pad1)
- U3 pad 3: unconnected-(U3-D4-Pad3) -> Net-(U2-O7)
- U3 pad 4: unconnected-(U3-D5-Pad4) -> Net-(J2-Pin_1)
- U3 pad 5: unconnected-(U3-D6-Pad5) -> GND
- U3 pad 7: unconnected-(U3-~{Q7}-Pad7) -> GND
- U3 pad 8: GND -> unconnected-(U3-Pad8)
- U3 pad 9: unconnected-(U3-Q7-Pad9) -> GND
- U4 pad 1: unconnected-(U4-~{PL}-Pad1) -> PMOD_IO4
- U4 pad 10: unconnected-(U4-DS-Pad10) -> Net-(U4-I1c)
- U4 pad 11: unconnected-(U4-D0-Pad11) -> Net-(U4-I0c)
- U4 pad 12: unconnected-(U4-D1-Pad12) -> PMOD_IO8
- U4 pad 13: unconnected-(U4-D2-Pad13) -> Net-(J2-Pin_2)
- U4 pad 14: unconnected-(U4-D3-Pad14) -> Net-(U4-I0d)
- U4 pad 15: unconnected-(U4-~{CE}-Pad15) -> GND
- U4 pad 16: +3V3 -> +3.3V
- U4 pad 2: unconnected-(U4-CP-Pad2) -> Net-(U4-I0a)
- U4 pad 3: unconnected-(U4-D4-Pad3) -> Net-(U4-I1a)
- U4 pad 4: unconnected-(U4-D5-Pad4) -> PMOD_IO5
- U4 pad 5: unconnected-(U4-D6-Pad5) -> Net-(U4-I0b)
- U4 pad 6: unconnected-(U4-D7-Pad6) -> Net-(U4-I1b)
- U4 pad 7: unconnected-(U4-~{Q7}-Pad7) -> PMOD_IO6
- U4 pad 9: unconnected-(U4-Q7-Pad9) -> PMOD_IO7
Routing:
- net Net-(SW55-Pad1): track 0.00 -> 271.4 mm, vias 0 -> 3
- net Net-(J2-Pin_2): track 0.00 -> 262.4 mm, vias 0 -> 2
- net +3.3V: track 0.00 -> 247.6 mm, vias 0 -> 3
- net Net-(U4-I0c): track 0.00 -> 234.8 mm, vias 0 -> 9
- net Net-(U4-I1a): track 0.00 -> 225.4 mm, vias 0 -> 4
- net Net-(J2-Pin_1): track 0.00 -> 215.4 mm, vias 0 -> 4
- net Net-(SW44-Pad2): track 0.00 -> 211.7 mm, vias 0 -> 1
- net Net-(U4-I0b): track 0.00 -> 210.5 mm, vias 0 -> 2
- net Net-(U4-I0d): track 0.00 -> 206.1 mm, vias 0 -> 4
- net Net-(U4-I1c): track 0.00 -> 197.1 mm, vias 0 -> 7
- net Net-(U4-I0a): track 0.00 -> 197.0 mm, vias 0 -> 7
- net Net-(SW28-Pad2): track 0.00 -> 188.5 mm, vias 0 -> 5
- net Net-(U4-I1b): track 0.00 -> 169.3 mm, vias 0 -> 5
- net GND: track 0.00 -> 162.6 mm
- net Net-(SW1-Pad2): track 0.00 -> 135.6 mm, vias 0 -> 2
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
